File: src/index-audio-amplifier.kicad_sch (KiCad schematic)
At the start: 45 parts, among them J1 USB_B_Micro, J2 SWD_PicoprobeCandybar, SW1 SW_Push, U1 RP2040, U2 RT6150B-33GQW, U3 W25Q16JVUXIQ, U4 MAX98360CENL, U5 TLV70033_SOT23-5, U6 MAX98360CENL, X1 12MHz

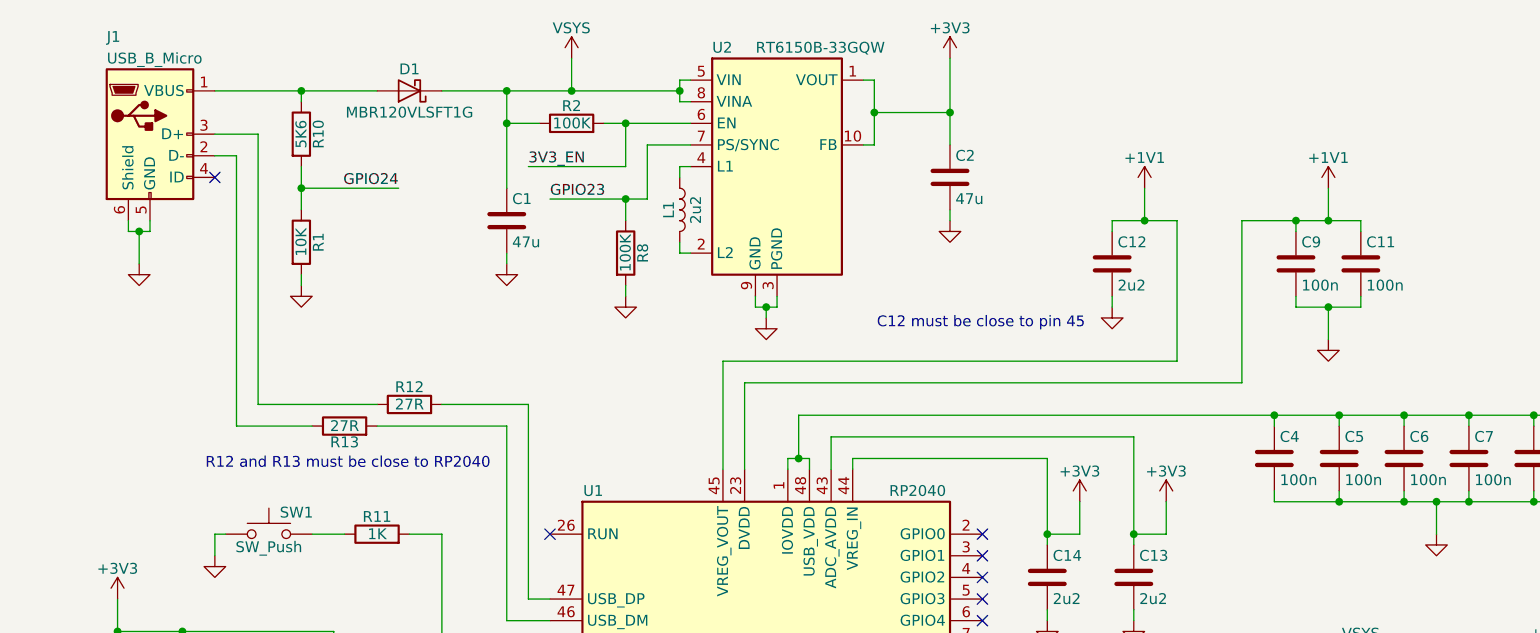
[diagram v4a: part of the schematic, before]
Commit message: Replace Micro-USB with USC-C
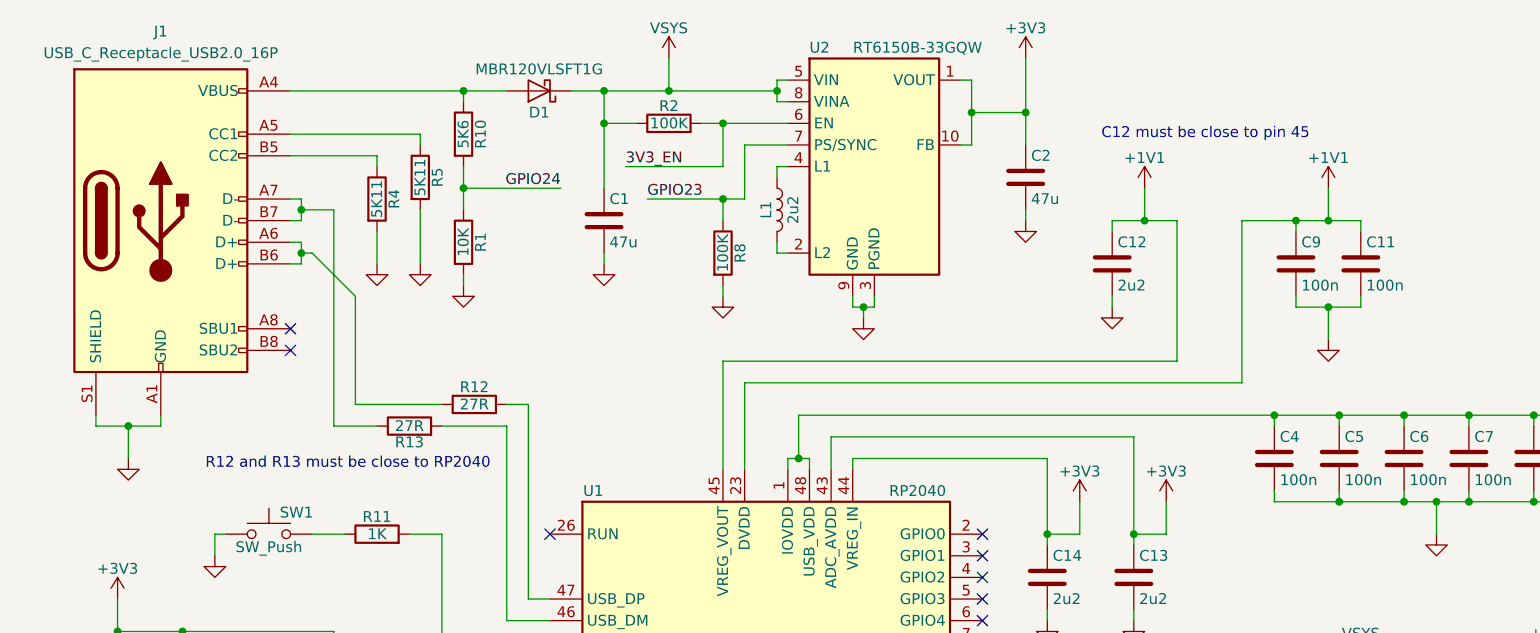
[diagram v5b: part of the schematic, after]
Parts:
- removed J1: USB_B_Micro, Connector_USB:USB_Micro-B_Amphenol_10103594-0001LF_Horizontal, symbol Connector:USB_B_Micro
- added J1: USB_C_Receptacle_USB2.0_16P, Connector_USB:USB_C_Receptacle_GCT_USB4105-xx-A_16P_TopMnt_Horizontal, symbol Connector:USB_C_Receptacle_USB2.0_16P
- added R4, R5: 5K11, Resistor_SMD:R_0402_1005Metric, symbol Device:R
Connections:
- net GND: now also J1.A1 (GND), J1.A12 (GND), J1.B1 (GND), J1.B12 (GND), J1.S1 (SHIELD), R4.2, R5.2
- net at R12.1: now also J1.A6 (D+), J1.B6 (D+)
- net at D1.2 (A), R10.1: now also J1.A4 (VBUS), J1.A9 (VBUS), J1.B4 (VBUS), J1.B9 (VBUS)
- net at R13.1: now also J1.A7 (D-), J1.B7 (D-)
- new net: J1.A5 (CC1), R5.1
- new net: J1.B5 (CC2), R4.1
- no-connect marks 25 -> 26
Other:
- moved on the sheet: C1, C2, D1, L1, R1, R10, R12, R13, R2, R8, U2

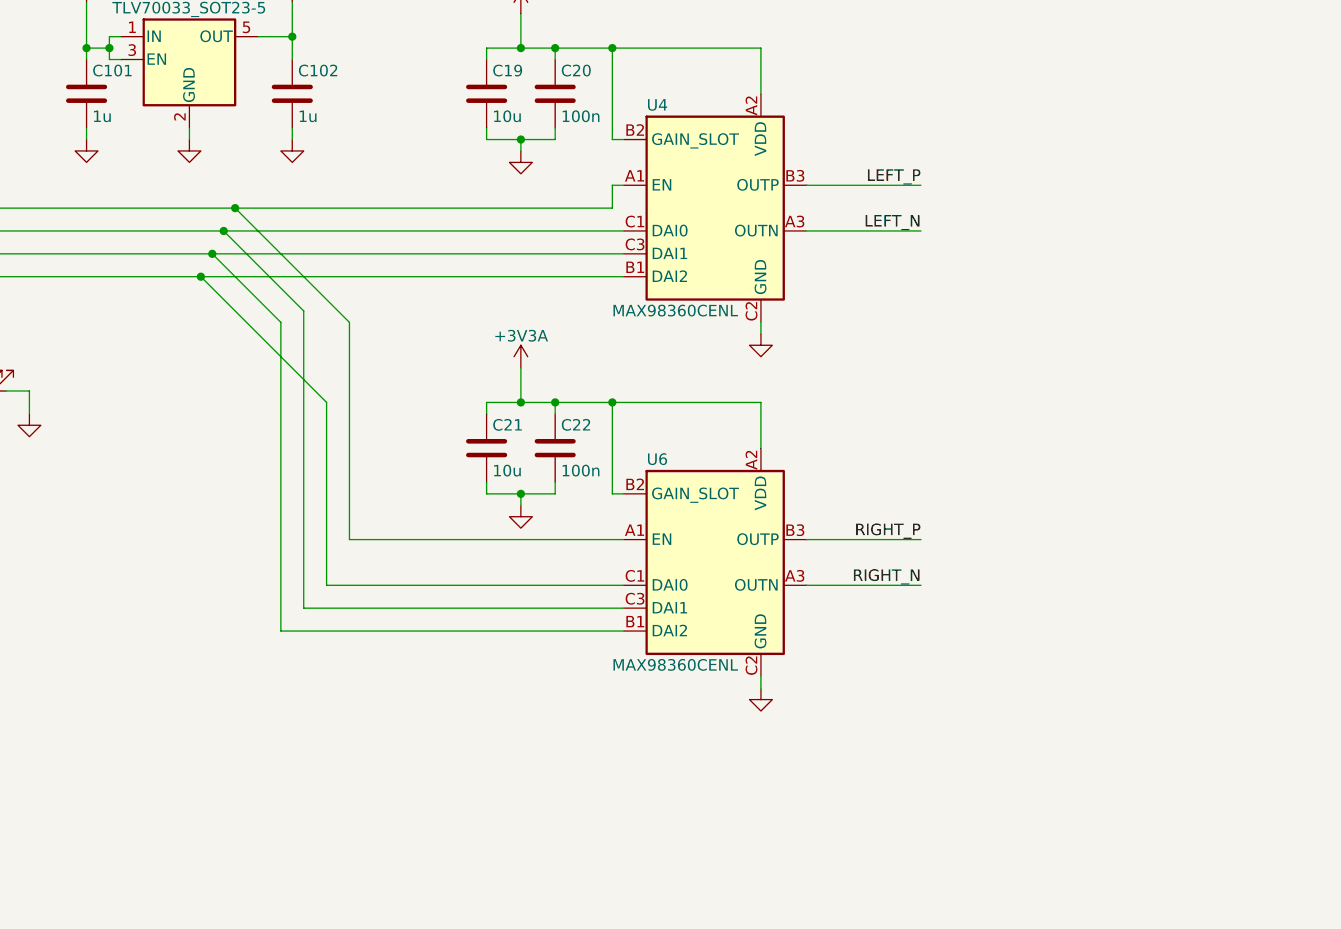
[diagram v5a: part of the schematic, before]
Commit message: Change audio GND to AGND; add MountingHole
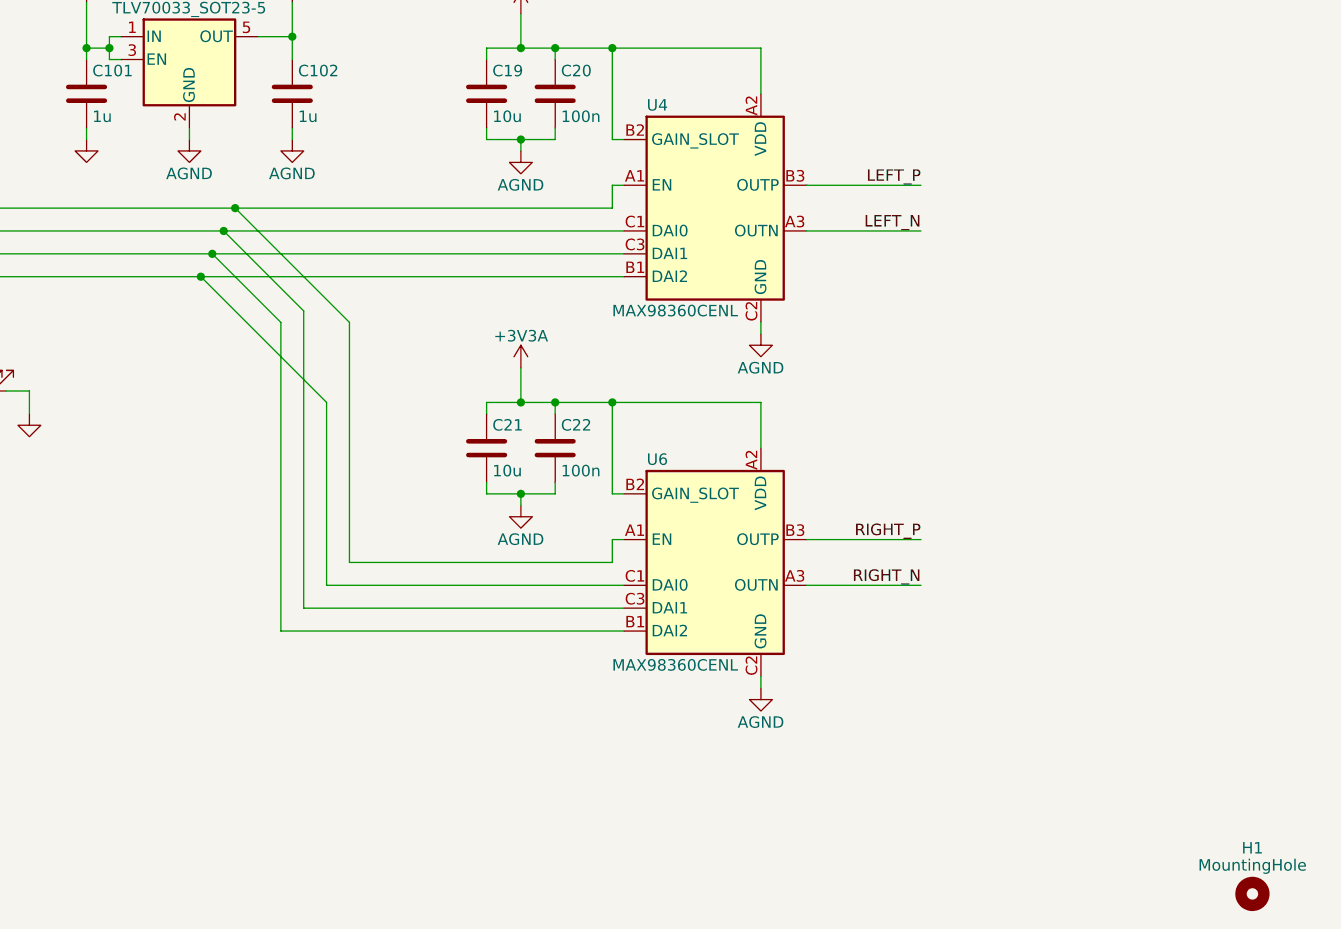
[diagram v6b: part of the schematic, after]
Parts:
- added H1: MountingHole, MountingHole:MountingHole_2.2mm_M2_ISO7380, symbol Mechanical:MountingHole
- U2: footprint Package_DFN_QFN:WDFN-10-1EP_3x3mm_P0.5mm_EP1.8x2.5mm_ThermalVias -> Package_SON:Texas_DRC0010J
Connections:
- net GND: no longer C102.2, C19.2, C20.2, C21.2, C22.2, U4.C2 (GND), U5.2 (GND), U6.C2 (GND)
- new net AGND: C102.2, C19.2, C20.2, C21.2, C22.2, U4.C2 (GND), U5.2 (GND), U6.C2 (GND)

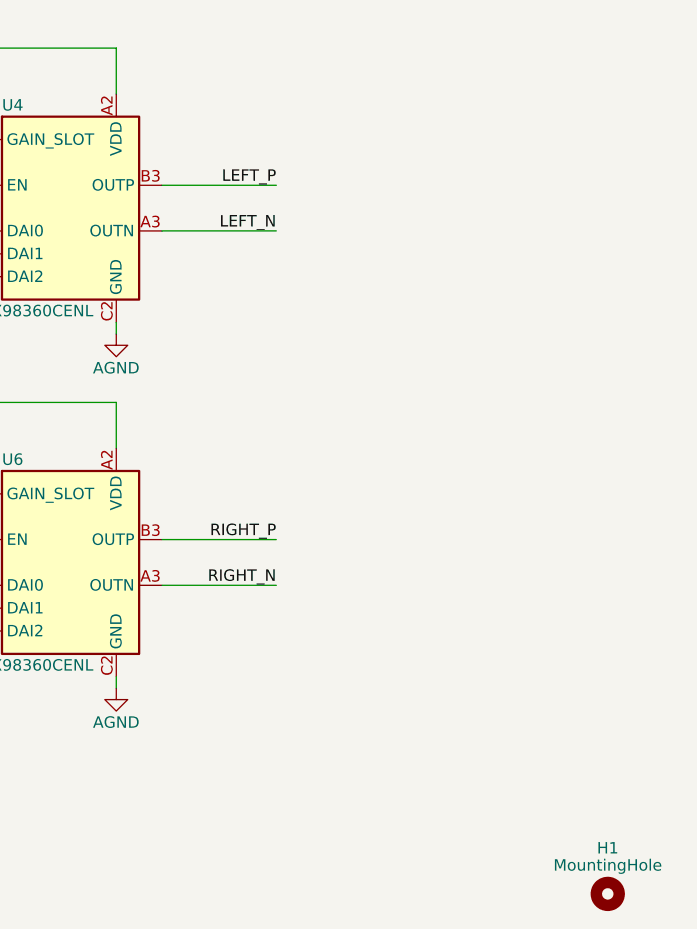
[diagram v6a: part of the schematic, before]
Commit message: Add connectors for speaker outputs
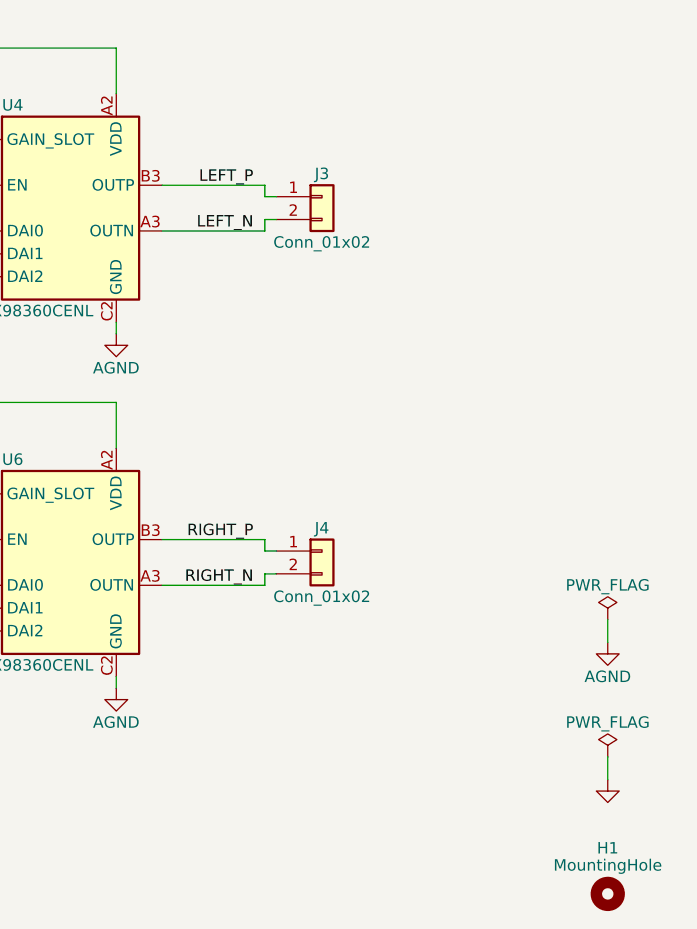
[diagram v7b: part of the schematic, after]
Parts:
- added J3, J4: Conn_01x02, symbol Connector_Generic:Conn_01x02
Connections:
- net LEFT_N: now also J3.2 (Pin_2)
- net LEFT_P: now also J3.1 (Pin_1)
- net RIGHT_N: now also J4.2 (Pin_2)
- net RIGHT_P: now also J4.1 (Pin_1)

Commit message: Change MAX98360CENL footprint to custom WLP-9
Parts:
- J3, J4: footprint (none) -> Connector_PinHeader_1.00mm:PinHeader_1x02_P1.00mm_Vertical
- U4, U6: footprint Package_BGA:WLP-9_1.468x1.448mm_Layout3x3_P0.4mm -> ProjectFootprints_IndexAudioAmplifier:WLP-9_1.347x1.347mm_Layout3x3_P0.4mm
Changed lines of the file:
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@@
 			)
 		)
-		(property "Footprint" ""
+		(property "Footprint" "Connector_PinHeader_1.00mm:PinHeader_1x02_P1.00mm_Vertical"
 			(at 275.59 157.48 0)
 			(effects
@@
 			)
 		)
-		(property "Footprint" ""
+		(property "Footprint" "Connector_PinHeader_1.00mm:PinHeader_1x02_P1.00mm_Vertical"
 			(at 275.59 118.11 0)
 			(effects
@@
 			)
 		)
-		(property "Footprint" "Package_BGA:WLP-9_1.468x1.448mm_Layout3x3_P0.4mm"
+		(property "Footprint" "ProjectFootprints_IndexAudioAmplifier:WLP-9_1.347x1.347mm_Layout3x3_P0.4mm"
 			(at 247.65 139.7 0)
 			(effects
@@
 			)
 		)
-		(property "Footprint" "Package_BGA:WLP-9_1.468x1.448mm_Layout3x3_P0.4mm"
+		(property "Footprint" "ProjectFootprints_IndexAudioAmplifier:WLP-9_1.347x1.347mm_Layout3x3_P0.4mm"
 			(at 247.65 179.07 0)
 			(effects
